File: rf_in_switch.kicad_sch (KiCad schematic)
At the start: 7 parts, among them P17 MMCX-J-P-H-ST-TH1, P18 CONUFL001-SMD-T, P24 CONUFL001-SMD-T, U31 QPC8010QTR7

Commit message: More minor tweaks and cleanups
Signed-off-by: Corey Minyard <corey@minyard.net>
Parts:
- P18: now not fitted; now left out of the parts list
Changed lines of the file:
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@@
 		(unit 1)
 		(exclude_from_sim no)
-		(in_bom yes)
+		(in_bom no)
 		(on_board yes)
-		(dnp no)
+		(dnp yes)
 		(property "Reference" "P18"
 			(at 110.49 88.9 0)

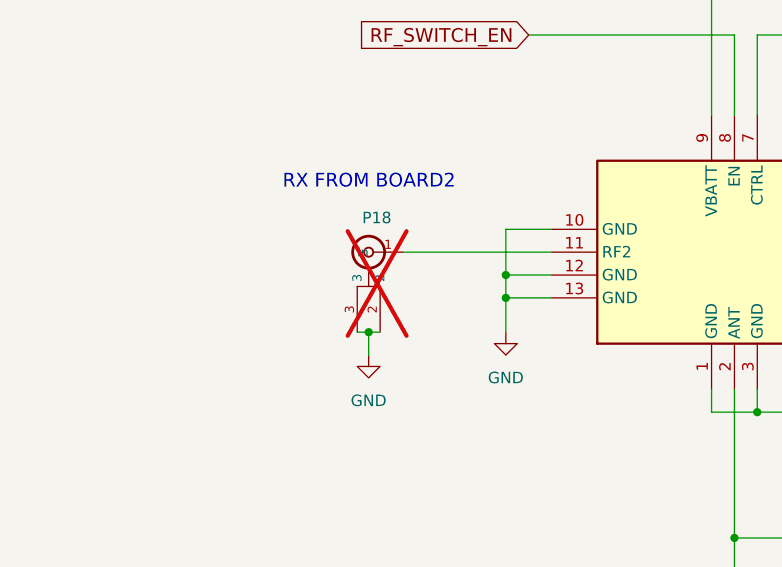
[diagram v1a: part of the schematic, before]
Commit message: Move the power LED to a better location
Not right in the middle of things, put it on the edge.

Signed-off-by: Corey Minyard <corey@minyard.net>
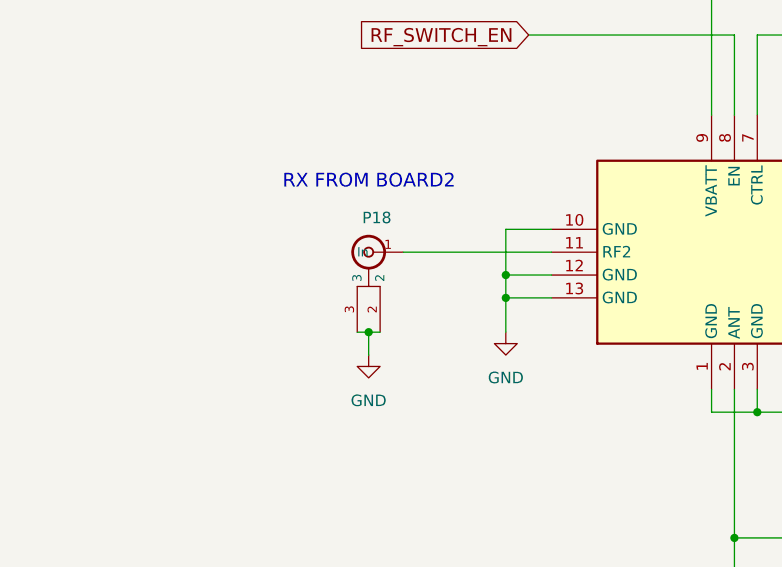
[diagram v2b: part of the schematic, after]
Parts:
- P18: now fitted; now in the parts list
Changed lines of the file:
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@@
 		(unit 1)
 		(exclude_from_sim no)
-		(in_bom no)
+		(in_bom yes)
 		(on_board yes)
-		(dnp yes)
+		(dnp no)
 		(property "Reference" "P18"
 			(at 110.49 88.9 0)

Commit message: Change MMCX connectors to right angle
There's not enough room on the board for vertical ones.

Signed-off-by: Corey Minyard <corey@minyard.net>
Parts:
- P17: value MMCX-J-P-H-ST-TH1 -> MMCX-J-P-H-RA-TH1; footprint PacSatDev_misc:COAX4_MMCX-J-P-H-ST-TH1_SAI -> PacSatDev_misc:COAX4_MMCX-J-P-H-RA-TH1_SAI; symbol PACSAT_DEV_misc:MMCX-J-P-H-ST-TH1 -> PACSAT_DEV_misc:MMCX-J-P-H-RA-TH1
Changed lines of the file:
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@@
 	)
 	(symbol
-		(lib_id "PACSAT_DEV_misc:MMCX-J-P-H-ST-TH1")
+		(lib_id "PACSAT_DEV_misc:MMCX-J-P-H-RA-TH1")
 		(at 153.67 147.32 0)
 		(unit 1)
@@
 			)
 		)
-		(property "Value" "MMCX-J-P-H-ST-TH1"
+		(property "Value" "MMCX-J-P-H-RA-TH1"
 			(at 153.67 147.32 0)
 			(effects
@@
 			)
 		)
-		(property "Footprint" "PacSatDev_misc:COAX4_MMCX-J-P-H-ST-TH1_SAI"
+		(property "Footprint" "PacSatDev_misc:COAX4_MMCX-J-P-H-RA-TH1_SAI"
 			(at 153.67 147.32 0)
 			(effects
@@
 			)
 		)
-		(property "Datasheet" "MMCX-J-P-H-ST-TH1"
+		(property "Datasheet" "MMCX-J-P-H-RA-TH1"
 			(at 153.67 147.32 0)
 			(effects

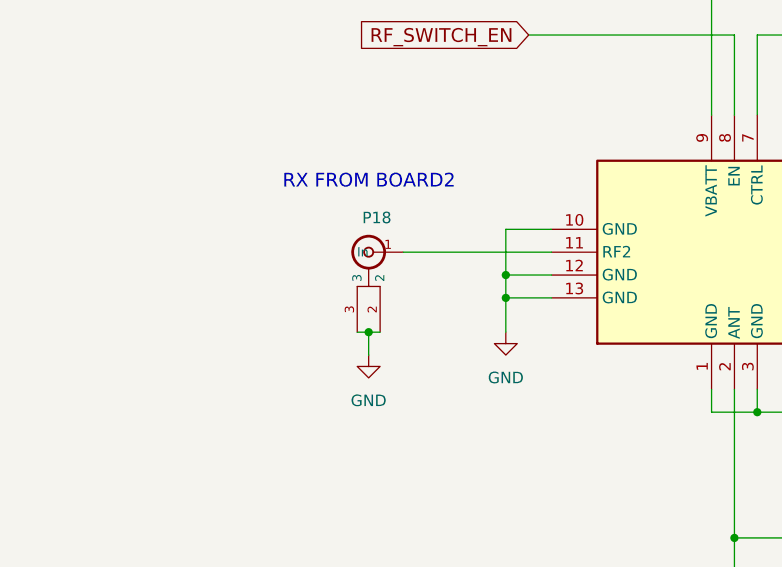
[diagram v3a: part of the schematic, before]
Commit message: Parts replacements for out of stock parts
Signed-off-by: Corey Minyard <corey@minyard.net>
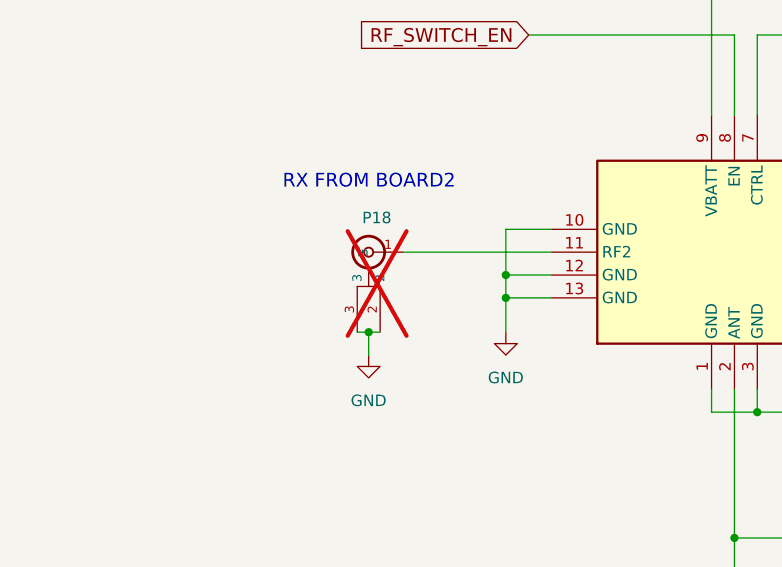
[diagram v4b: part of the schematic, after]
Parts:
- P18: now not fitted; now left out of the parts list
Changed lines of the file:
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@@
 		(unit 1)
 		(exclude_from_sim no)
-		(in_bom yes)
+		(in_bom no)
 		(on_board yes)
-		(dnp no)
+		(dnp yes)
 		(property "Reference" "P18"
 			(at 110.49 88.9 0)

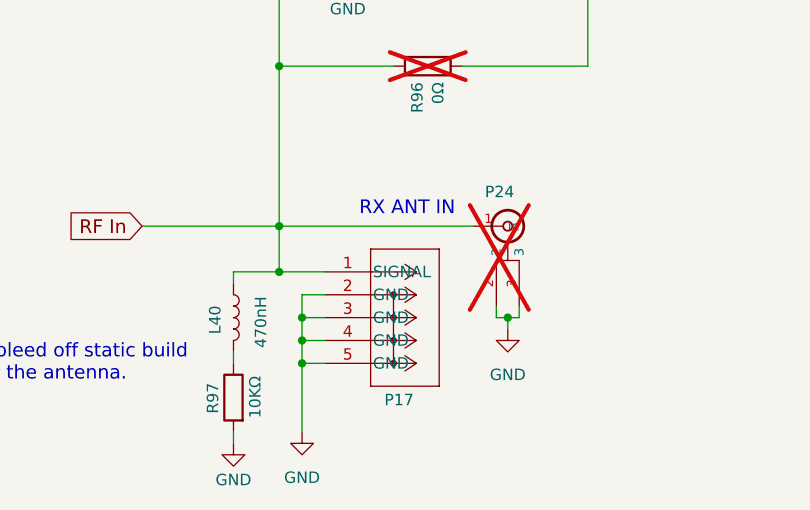
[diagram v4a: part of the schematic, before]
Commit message: Fix issues with the RF connectors
Remove the U.FL connectors P23, P24, and P26 they just weren't going
to work and there's no good place to put them, and where they were was
shorting the MMCX connectors.  Just use the MMCX ones for output.

Move the diplexer MMCX connector to give it more room and get it a
little more out of the way of the transmit connector.

Signed-off-by: Corey Minyard <corey@minyard.net>
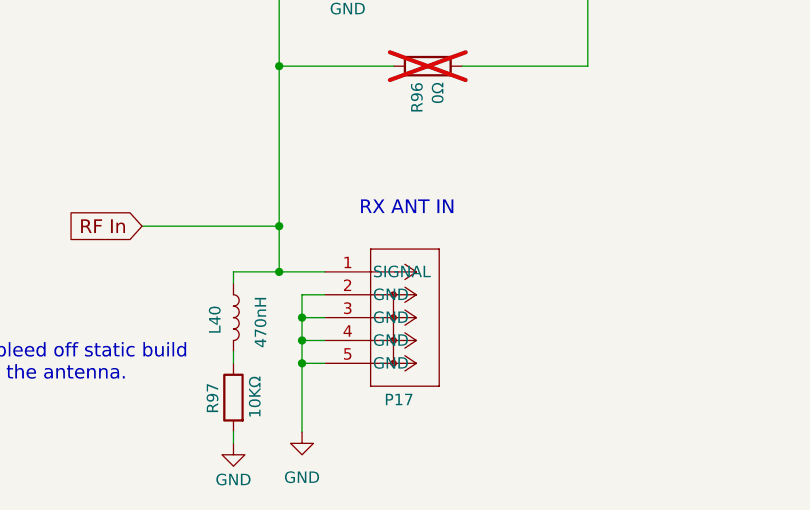
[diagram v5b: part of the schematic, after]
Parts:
- removed P24: CONUFL001-SMD-T, PacSatDev_misc:CONN1_CONUFL_TEC, symbol PACSAT_DEV_misc:U_FL
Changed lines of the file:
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@@
-	)
-	(junction
-		(at 173.99 152.4)
-		(diameter 0)
-		(color 0 0 0 0)
 	)
 	(junction
@@
 	(wire
 		(pts
-			(xy 172.72 151.13) (xy 172.72 152.4)
-		)
-		(stroke
-			(width 0)
-			(type default)
-		)
-	)
-	(wire
-		(pts
 			(xy 172.72 68.58) (xy 151.13 68.58)
 		)
@@
 	(wire
 		(pts
-			(xy 173.99 152.4) (xy 172.72 152.4)
-		)
-		(stroke
-			(width 0)
-			(type default)
-		)
-	)
-	(wire
-		(pts
 			(xy 123.19 95.25) (xy 128.27 95.25)
 		)
@@
 	(wire
 		(pts
-			(xy 175.26 152.4) (xy 173.99 152.4)
-		)
-		(stroke
-			(width 0)
-			(type default)
-		)
-	)
-	(wire
-		(pts
 			(xy 143.51 147.32) (xy 148.59 147.32)
 		)
@@
 	(wire
 		(pts
-			(xy 173.99 153.67) (xy 173.99 152.4)
-		)
-		(stroke
-			(width 0)
-			(type default)
-		)
-	)
-	(wire
-		(pts
 			(xy 161.29 124.46) (xy 148.59 124.46)
 		)
@@
 	(wire
 		(pts
-			(xy 170.18 142.24) (xy 148.59 142.24)
-		)
-		(stroke
-			(width 0)
-			(type default)
-		)
-	)
-	(wire
-		(pts
 			(xy 123.19 97.79) (xy 123.19 95.25)
 		)
@@
 		(pts
 			(xy 151.13 110.49) (xy 146.05 110.49)
-		)
-		(stroke
-			(width 0)
-			(type default)
-		)
-	)
-	(wire
-		(pts
-			(xy 175.26 151.13) (xy 175.26 152.4)
 		)
 		(stroke
@@
 	)
 	(symbol
-		(lib_id "power:GND")
-		(at 173.99 153.67 0)
-		(mirror y)
-		(unit 1)
-		(exclude_from_sim no)
-		(in_bom yes)
-		(on_board yes)
-		(dnp no)
-		(fields_autoplaced yes)
-		(property "Reference" "#PWR0253"
-			(at 173.99 160.02 0)
-			(effects
-				(font
-					(size 1.27 1.27)
-				)
-				(hide yes)
-			)
-		)
-		(property "Value" "GND"
-			(at 173.99 158.75 0)
-			(effects
-				(font
-					(size 1.27 1.27)
-				)
-			)
-		)
-		(property "Footprint" ""
-			(at 173.99 153.67 0)
-			(effects
-				(font
-					(size 1.27 1.27)
-				)
-				(hide yes)
-			)
-		)
-		(property "Datasheet" ""
-			(at 173.99 153.67 0)
-			(effects
-				(font
-					(size 1.27 1.27)
-				)
-				(hide yes)
-			)
-		)
-		(property "Description" ""
-			(at 173.99 153.67 0)
-			(effects
-				(font
-					(size 1.27 1.27)
-				)
-			)
-		)
-		(pin "1"
-		)
-		(instances
-			(project "PacSat_AFSK"
-				(path "/cc9f42d2-6985-41ac-acab-5ab7b01c5b38/4fa888af-703c-49ed-93bb-d56d2f02c470/64a91b23-a882-4658-bea9-c6c8274e2ac4"
-					(reference "#PWR0253")
-					(unit 1)
-				)
-			)
-		)
-	)
-	(symbol
 		(lib_id "power:+5V")
 		(at 146.05 58.42 0)
@@
 					(unit 1)
 				)
-			)
-		)
-	)
-	(symbol
-		(lib_id "PACSAT_DEV_misc:U_FL")
-		(at 173.99 142.24 0)
-		(unit 1)
-		(exclude_from_sim no)
-		(in_bom no)
-		(on_board yes)
-		(dnp yes)
-		(property "Reference" "P24"
-			(at 171.45 138.43 0)
-			(effects
-				(font
-					(size 1.27 1.27)
-				)
-				(justify left)
-			)
-		)
-		(property "Value" "CONUFL001-SMD-T"
-			(at 173.99 142.24 0)
-			(effects
-				(font
-					(size 1.27 1.27)
-				)
-				(hide yes)
-			)
-		)
-		(property "Footprint" "PacSatDev_misc:CONN1_CONUFL_TEC"
-			(at 173.99 142.24 0)
-			(effects
-				(font
-					(size 1.27 1.27)
-				)
-				(hide yes)
-			)
-		)
-		(property "Datasheet" ""
-			(at 173.99 142.24 0)
-			(effects
-				(font
-					(size 1.27 1.27)
-				)
-				(hide yes)
-			)
-		)
-		(property "Description" ""
-			(at 173.99 142.24 0)
-			(effects
-				(font
-					(size 1.27 1.27)
-				)
-			)
-		)
-		(pin "1"
-		)
-		(pin "2"
-		)
-		(pin "3"
-		)
-		(instances
-			(project "PacSat_AFSK"
-				(path "/cc9f42d2-6985-41ac-acab-5ab7b01c5b38/4fa888af-703c-49ed-93bb-d56d2f02c470/64a91b23-a882-4658-bea9-c6c8274e2ac4"
-					(reference "P24")
-					(unit 1)
-				)
